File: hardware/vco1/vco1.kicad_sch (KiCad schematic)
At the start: 77 parts, among them J1 AudioJack2_SwitchT, J10 Conn_01x02_Pin, J2 AudioJack2_SwitchT, J3 AudioJack2_SwitchT, J4 AudioJack2_SwitchT, J5 Conn_02x08_Odd_Even, J6 AudioJack2_SwitchT, J7 AudioJack2_SwitchT, J8 Conn_01x02_Pin, J9 Conn_01x02_Pin, Q1 2N3904, Q2 2N3906, U1 40106, U2 TL074, U3 TL074

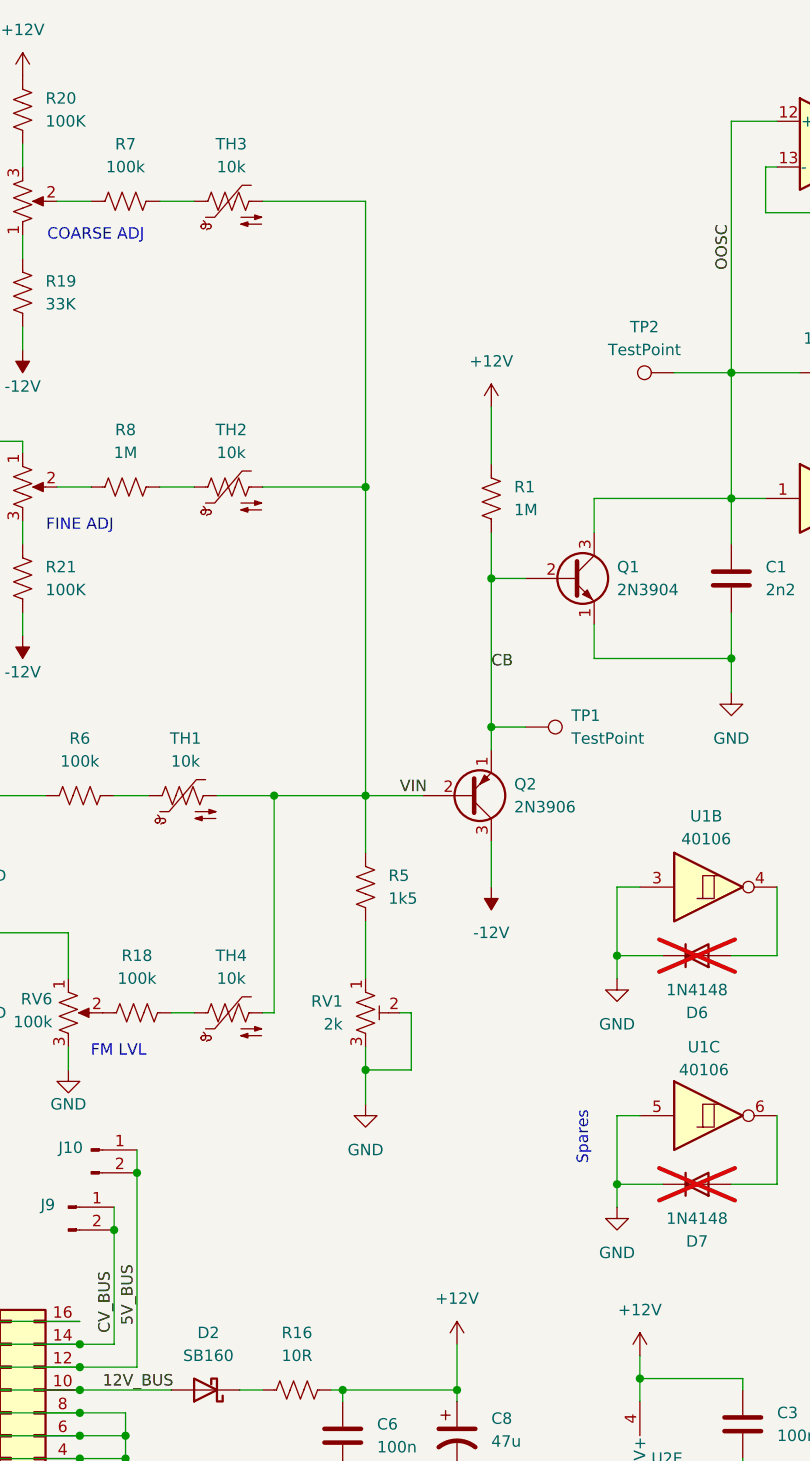
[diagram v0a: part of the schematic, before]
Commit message: added more test points and documentation. Currently cannot adjust to f_osc < 800Hz
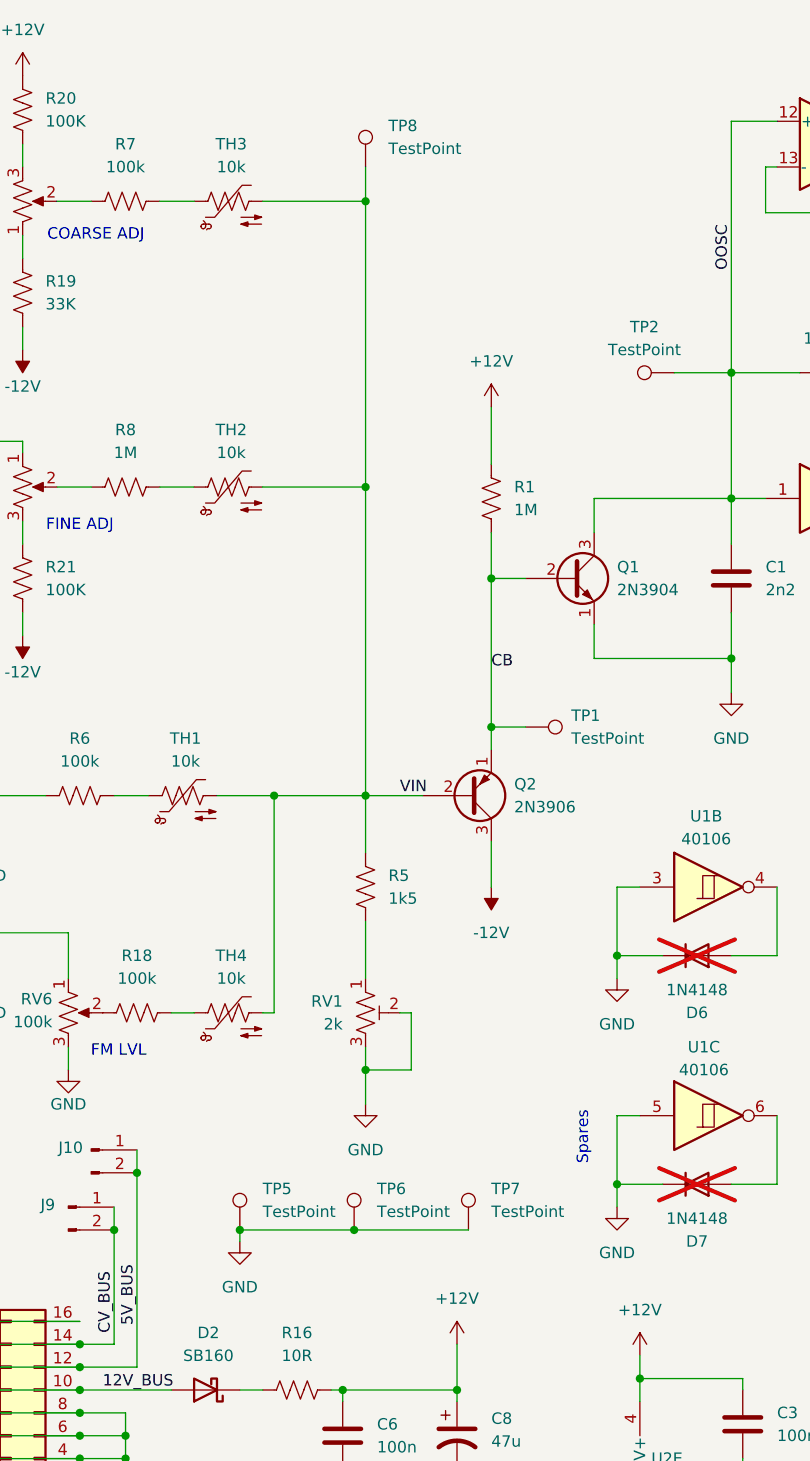
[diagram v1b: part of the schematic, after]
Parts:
- added TP5, TP6, TP7, TP8: TestPoint, Connector_PinHeader_2.54mm:PinHeader_1x01_P2.54mm_Vertical, symbol Connector:TestPoint
- TP1, TP2, TP3, TP4: footprint Connector_PinHeader_1.00mm:PinHeader_1x01_P1.00mm_Vertical -> Connector_PinHeader_2.54mm:PinHeader_1x01_P2.54mm_Vertical
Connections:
- net GND: now also TP5.1, TP6.1, TP7.1
- net VIN: now also TP8.1

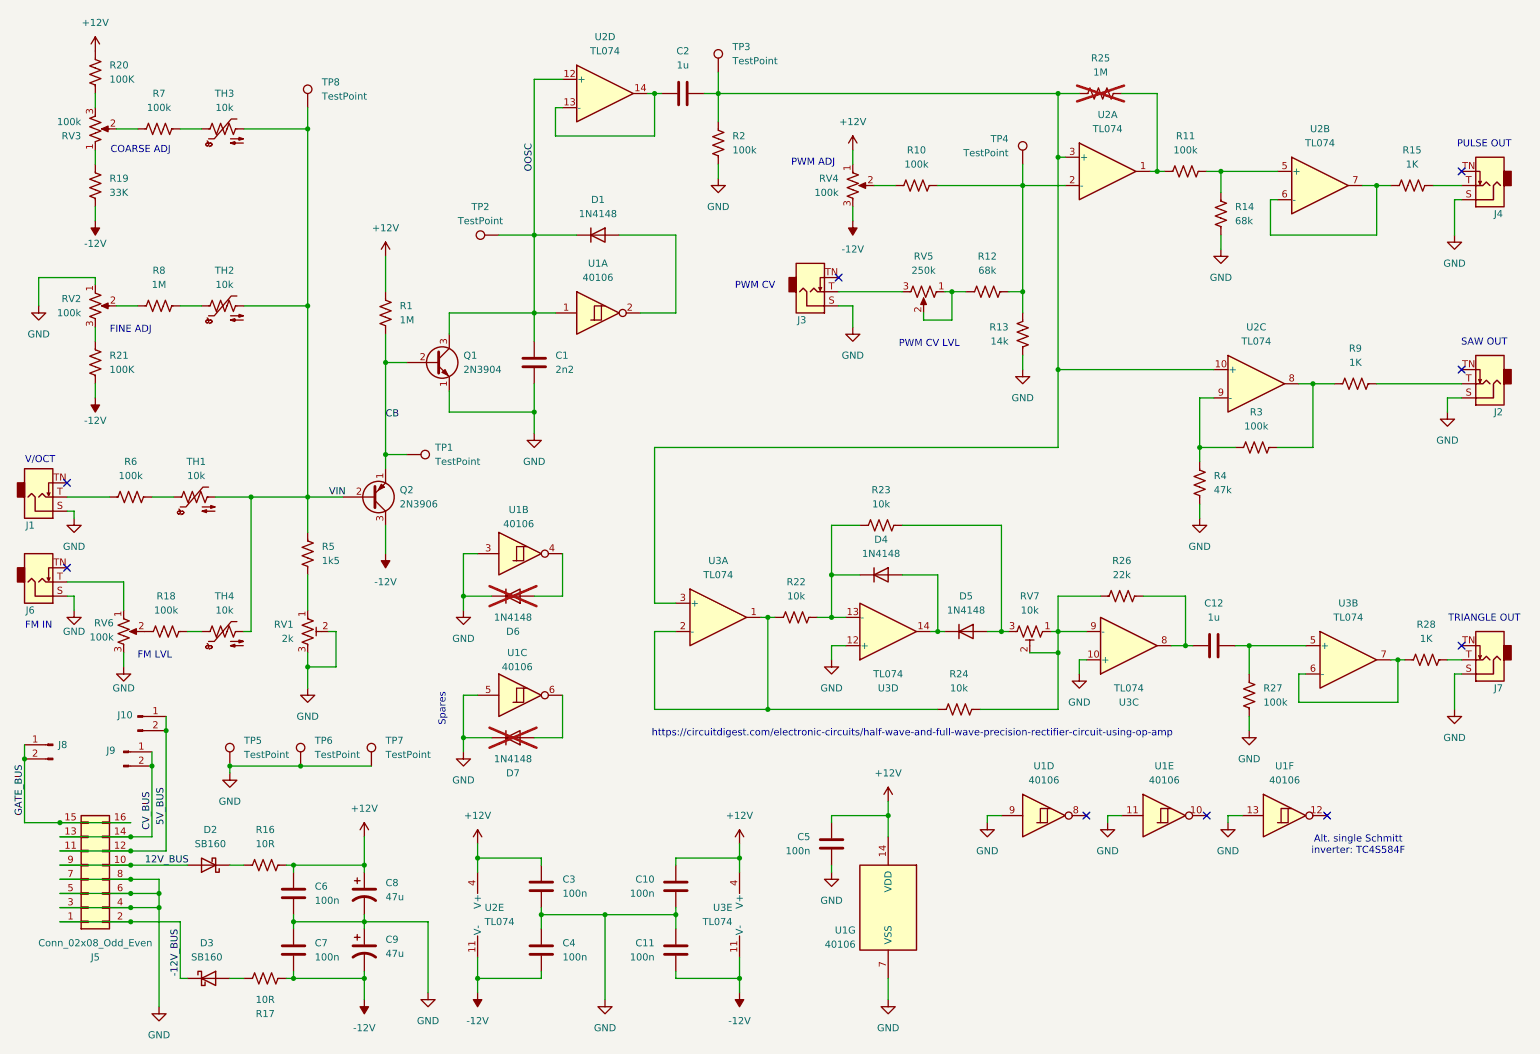
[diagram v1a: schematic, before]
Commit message: Update schematic and board to v1.1 based on initial test from v1 PCB. Changes in README.md
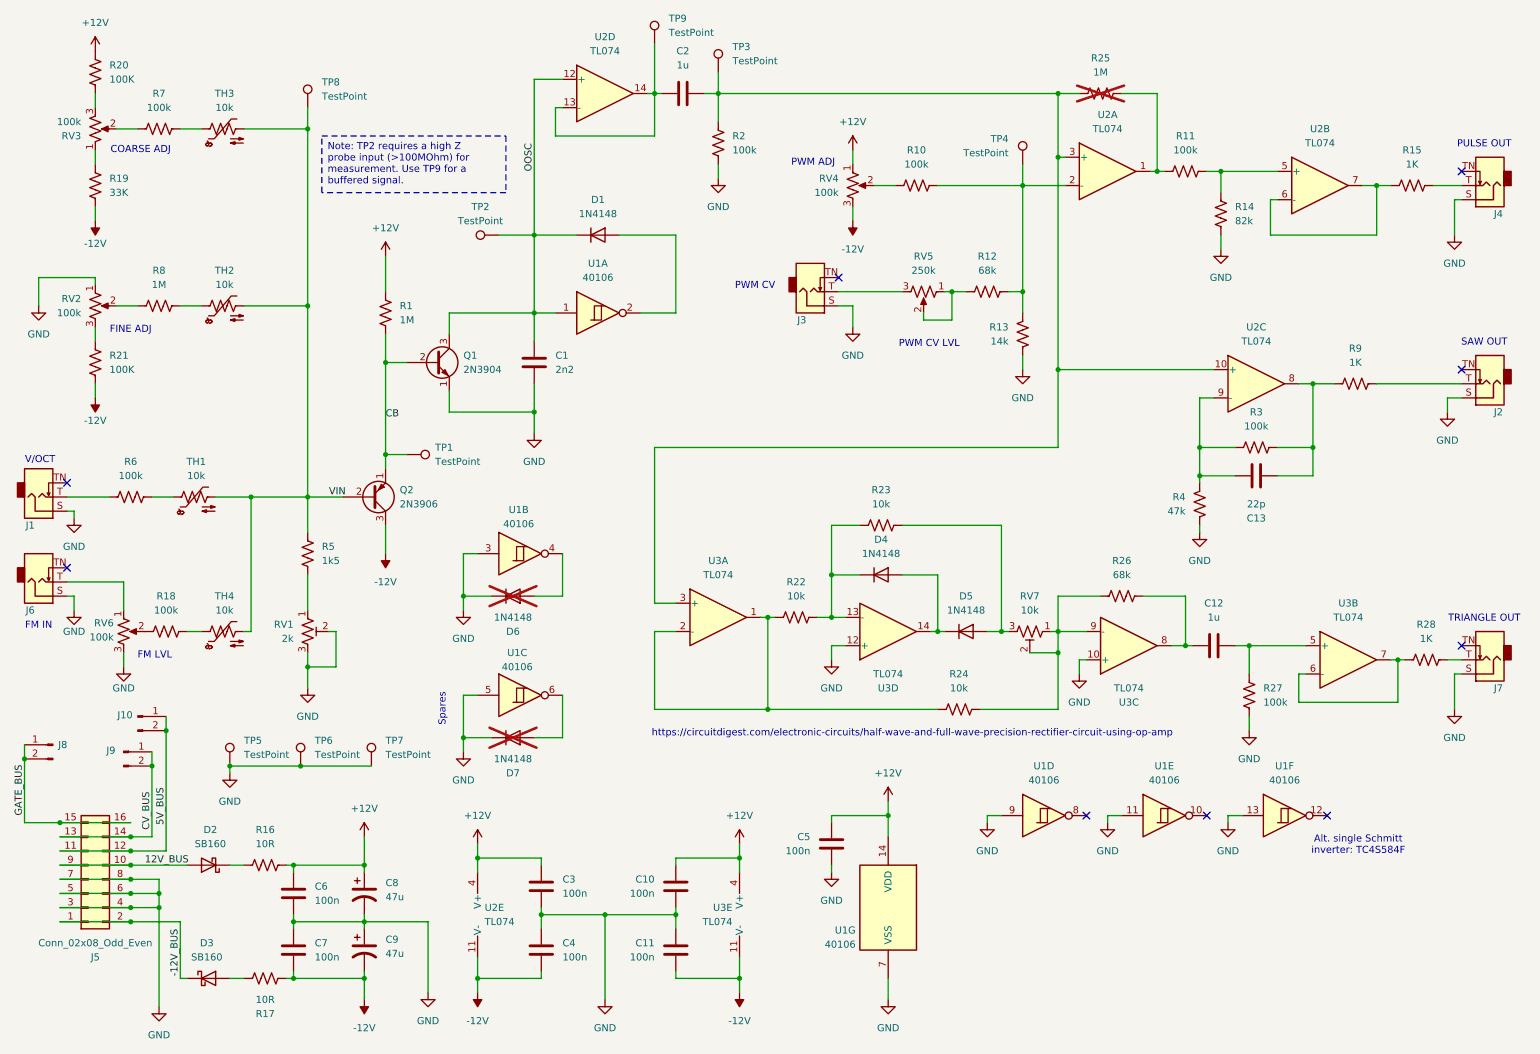
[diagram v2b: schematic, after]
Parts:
- added C13: 22p, Capacitor_THT:C_Disc_D5.0mm_W2.5mm_P5.00mm, symbol Device:C
- added TP9: TestPoint, Connector_PinHeader_2.54mm:PinHeader_1x01_P2.54mm_Vertical, symbol Connector:TestPoint
- R14: value 68k -> 82k
- R26: value 22k -> 68k
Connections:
- net at R3.2, R9.1, U2.8: now also C13.2
- net at R3.1, R4.2, U2.9 (-): now also C13.1
- net at C2.1, U2.13 (-), U2.14: now also TP9.1
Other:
- moved on the sheet: R4
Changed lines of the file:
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@@
 	(title_block
 		(title "Sawtooth Core VCO")
-		(date "2024-07-09")
-		(rev "1")
+		(date "2024-07-26")
+		(rev "1.1")
 		(company "idyllm")
 		(comment 1 "CC BY-SA 4.0")
@@
 	)
 	(junction
+		(at 246.38 91.44)
+		(diameter 0)
+		(color 0 0 0 0)
+	)
+	(junction
 		(at 257.81 44.45)
 		(diameter 0)
@@
 	)
 	(junction
+		(at 226.06 96.52)
+		(diameter 0)
+		(color 0 0 0 0)
+	)
+	(junction
 		(at 261.62 129.54)
 		(diameter 0)
@@
 	(wire
 		(pts
+			(xy 226.06 96.52) (xy 232.41 96.52)
+		)
+		(stroke
+			(width 0)
+			(type default)
+		)
+	)
+	(wire
+		(pts
 			(xy 194.31 44.45) (xy 201.93 44.45)
 		)
@@
 	(wire
 		(pts
+			(xy 226.06 96.52) (xy 226.06 91.44)
+		)
+		(stroke
+			(width 0)
+			(type default)
+		)
+	)
+	(wire
+		(pts
 			(xy 160.02 127) (xy 162.56 127)
 		)
@@
 	(wire
 		(pts
+			(xy 240.03 96.52) (xy 246.38 96.52)
+		)
+		(stroke
+			(width 0)
+			(type default)
+		)
+	)
+	(wire
+		(pts
 			(xy 27.94 80.01) (xy 27.94 82.55)
 		)
@@
 	(wire
 		(pts
+			(xy 128.27 19.05) (xy 128.27 27.94)
+		)
+		(stroke
+			(width 0)
+			(type default)
+		)
+	)
+	(wire
+		(pts
 			(xy 31.75 66.04) (xy 35.56 66.04)
 		)
@@
 	(wire
 		(pts
-			(xy 226.06 104.14) (xy 226.06 101.6)
+			(xy 226.06 106.68) (xy 226.06 105.41)
 		)
 		(stroke
@@
 	(wire
 		(pts
+			(xy 246.38 96.52) (xy 246.38 91.44)
+		)
+		(stroke
+			(width 0)
+			(type default)
+		)
+	)
+	(wire
+		(pts
 			(xy 34.29 166.37) (xy 44.45 166.37)
 		)
@@
 	(wire
 		(pts
-			(xy 226.06 93.98) (xy 226.06 91.44)
+			(xy 226.06 97.79) (xy 226.06 96.52)
 		)
 		(stroke
@@
 		)
 	)
+	(text_box "Note: TP2 requires a high Z probe input (>100MOhm) for measurement. Use TP9 for a buffered signal."
+		(exclude_from_sim no)
+		(at 68.58 35.56 0)
+		(size 33.02 10.16)
+		(stroke
+			(width 0)
+			(type dash)
+		)
+		(fill
+			(type none)
+		)
+		(effects
+			(font
+				(size 1.27 1.27)
+			)
+			(justify left top)
+		)
+	)
 	(text "TRIANGLE OUT"
 		(exclude_from_sim no)
@@
 			)
 		)
-		(property "Value" "22k"
+		(property "Value" "68k"
 			(at 212.09 114.3 90)
 			(effects
@@
 			)
 		)
-		(property "Value" "68k"
+		(property "Value" "82k"
 			(at 232.41 50.7999 0)
 			(effects
@@
 	(symbol
 		(lib_id "Device:R_US")
-		(at 226.06 97.79 180)
+		(at 226.06 101.6 0)
+		(mirror x)
 		(unit 1)
 		(exclude_from_sim no)
@@
 		(on_board yes)
 		(dnp no)
-		(fields_autoplaced yes)
 		(property "Reference" "R4"
-			(at 228.6 96.5199 0)
+			(at 223.52 100.3299 0)
 			(effects
 				(font
@@
 		)
 		(property "Value" "47k"
-			(at 228.6 99.0599 0)
+			(at 223.52 102.8699 0)
 			(effects
 				(font
@@
 		)
 		(property "Footprint" "Resistor_THT:R_Axial_DIN0204_L3.6mm_D1.6mm_P2.54mm_Vertical"
-			(at 225.044 97.536 90)
+			(at 227.076 101.346 90)
 			(effects
 				(font
@@
 		)
 		(property "Datasheet" "~"
-			(at 226.06 97.79 0)
+			(at 226.06 101.6 0)
 			(effects
 				(font
@@
 		)
 		(property "Description" "Resistor, US symbol"
-			(at 226.06 97.79 0)
+			(at 226.06 101.6 0)
 			(effects
 				(font
@@
 	)
 	(symbol
+		(lib_id "Connector:TestPoint")
+		(at 128.27 19.05 0)
+		(mirror y)
+		(unit 1)
+		(exclude_from_sim no)
+		(in_bom yes)
+		(on_board yes)
+		(dnp no)
+		(fields_autoplaced yes)
+		(property "Reference" "TP9"
+			(at 130.81 14.4779 0)
+			(effects
+				(font
+					(size 1.27 1.27)
+				)
+				(justify right)
+			)
+		)
+		(property "Value" "TestPoint"
+			(at 130.81 17.0179 0)
+			(effects
+				(font
+					(size 1.27 1.27)
+				)
+				(justify right)
+			)
+		)
+		(property "Footprint" "Connector_PinHeader_2.54mm:PinHeader_1x01_P2.54mm_Vertical"
+			(at 123.19 19.05 0)
+			(effects
+				(font
+					(size 1.27 1.27)
+				)
+				(hide yes)
+			)
+		)
+		(property "Datasheet" "~"
+			(at 123.19 19.05 0)
+			(effects
+				(font
+					(size 1.27 1.27)
+				)
+				(hide yes)
+			)
+		)
+		(property "Description" "test point"
+			(at 128.27 19.05 0)
+			(effects
+				(font
+					(size 1.27 1.27)
+				)
+				(hide yes)
+			)
+		)
+		(pin "1"
+		)
+		(instances
+			(project "vco1"
+				(path "/2e954017-059f-458a-b10a-31dfd5ac2991"
+					(reference "TP9")
+					(unit 1)
+				)
+			)
+		)
+	)
+	(symbol
 		(lib_id "power:GND")
 		(at 163.83 69.85 0)
@@
 	)
 	(symbol
+		(lib_id "Device:C")
+		(at 236.22 96.52 90)
+		(unit 1)
+		(exclude_from_sim no)
+		(in_bom yes)
+		(on_board yes)
+		(dnp no)
+		(property "Reference" "C13"
+			(at 236.22 104.14 90)
+			(effects
+				(font
+					(size 1.27 1.27)
+				)
+			)
+		)
+		(property "Value" "22p"
+			(at 236.22 101.6 90)
+			(effects
+				(font
+					(size 1.27 1.27)
+				)
+			)
+		)
+		(property "Footprint" "Capacitor_THT:C_Disc_D5.0mm_W2.5mm_P5.00mm"
+			(at 240.03 95.5548 0)
+			(effects
+				(font
+					(size 1.27 1.27)
+				)
+				(hide yes)
+			)
+		)
+		(property "Datasheet" "~"
+			(at 236.22 96.52 0)
+			(effects
+				(font
+					(size 1.27 1.27)
+				)
+				(hide yes)
+			)
+		)
+		(property "Description" "Unpolarized capacitor"
+			(at 236.22 96.52 0)
+			(effects
+				(font
+					(size 1.27 1.27)
+				)
+				(hide yes)
+			)
+		)
+		(pin "1"
+		)
+		(pin "2"
+		)
+		(instances
+			(project "vco1"
+				(path "/2e954017-059f-458a-b10a-31dfd5ac2991"
+					(reference "C13")
+					(unit 1)
+				)
+			)
+		)
+	)
+	(symbol
 		(lib_id "power:GND")
-		(at 226.06 104.14 0)
+		(at 226.06 106.68 0)
 		(unit 1)
 		(exclude_from_sim no)
@@
 		(fields_autoplaced yes)
 		(property "Reference" "#PWR05"
-			(at 226.06 110.49 0)
+			(at 226.06 113.03 0)
 			(effects
 				(font
@@
 		)
 		(property "Value" "GND"
-			(at 226.06 109.22 0)
+			(at 226.06 111.76 0)
 			(effects
 				(font
@@
 		)
 		(property "Footprint" ""
-			(at 226.06 104.14 0)
+			(at 226.06 106.68 0)
 			(effects
 				(font
@@
 		)
 		(property "Datasheet" ""
-			(at 226.06 104.14 0)
+			(at 226.06 106.68 0)
 			(effects
 				(font
@@
 		)
 		(property "Description" "Power symbol creates a global label with name \"GND\" , ground"
-			(at 226.06 104.14 0)
+			(at 226.06 106.68 0)
 			(effects
 				(font
